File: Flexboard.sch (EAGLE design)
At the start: 353 parts, among them U1 MK20DN512VLQ10

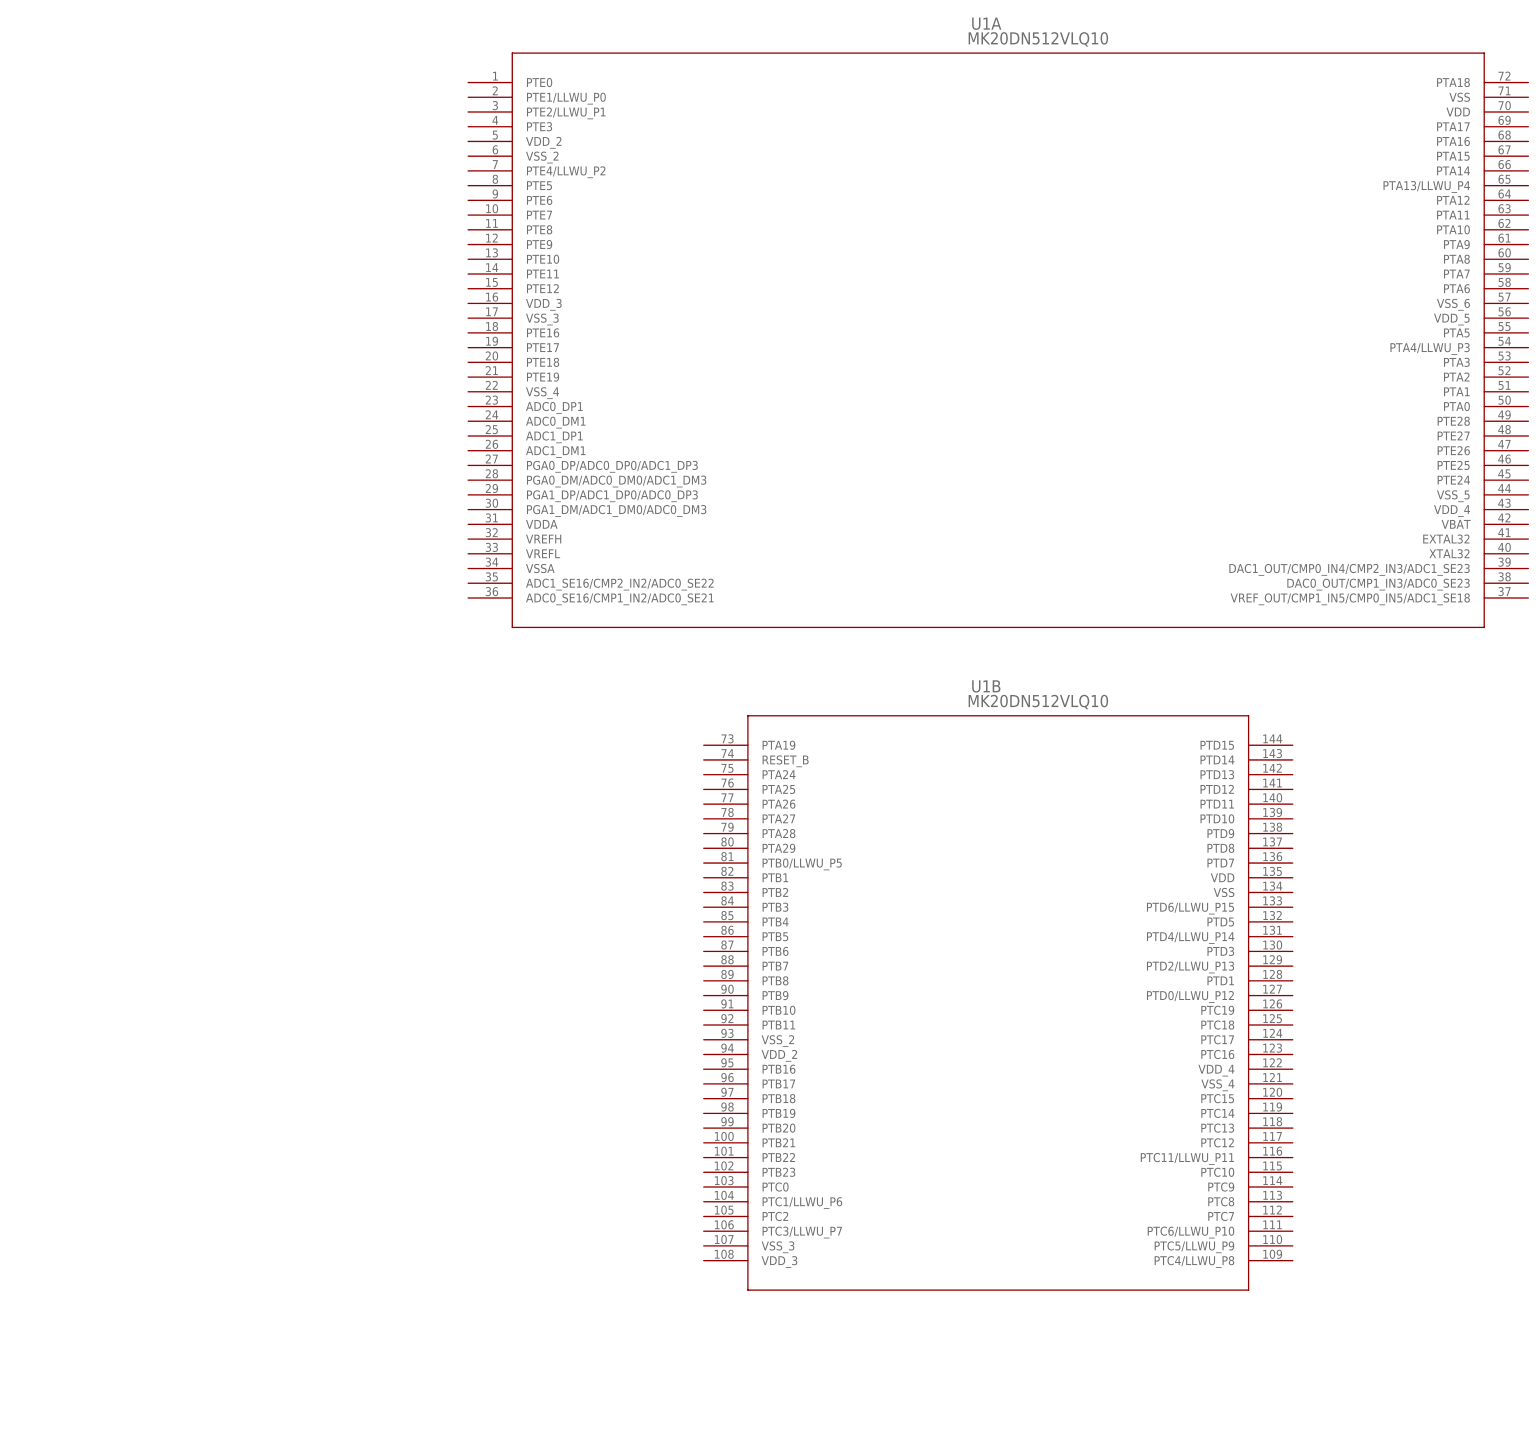
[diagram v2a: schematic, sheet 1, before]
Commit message: Assigned all keyboard traces to pins on MCU
All traces for columns and rows now have initial pin assignments
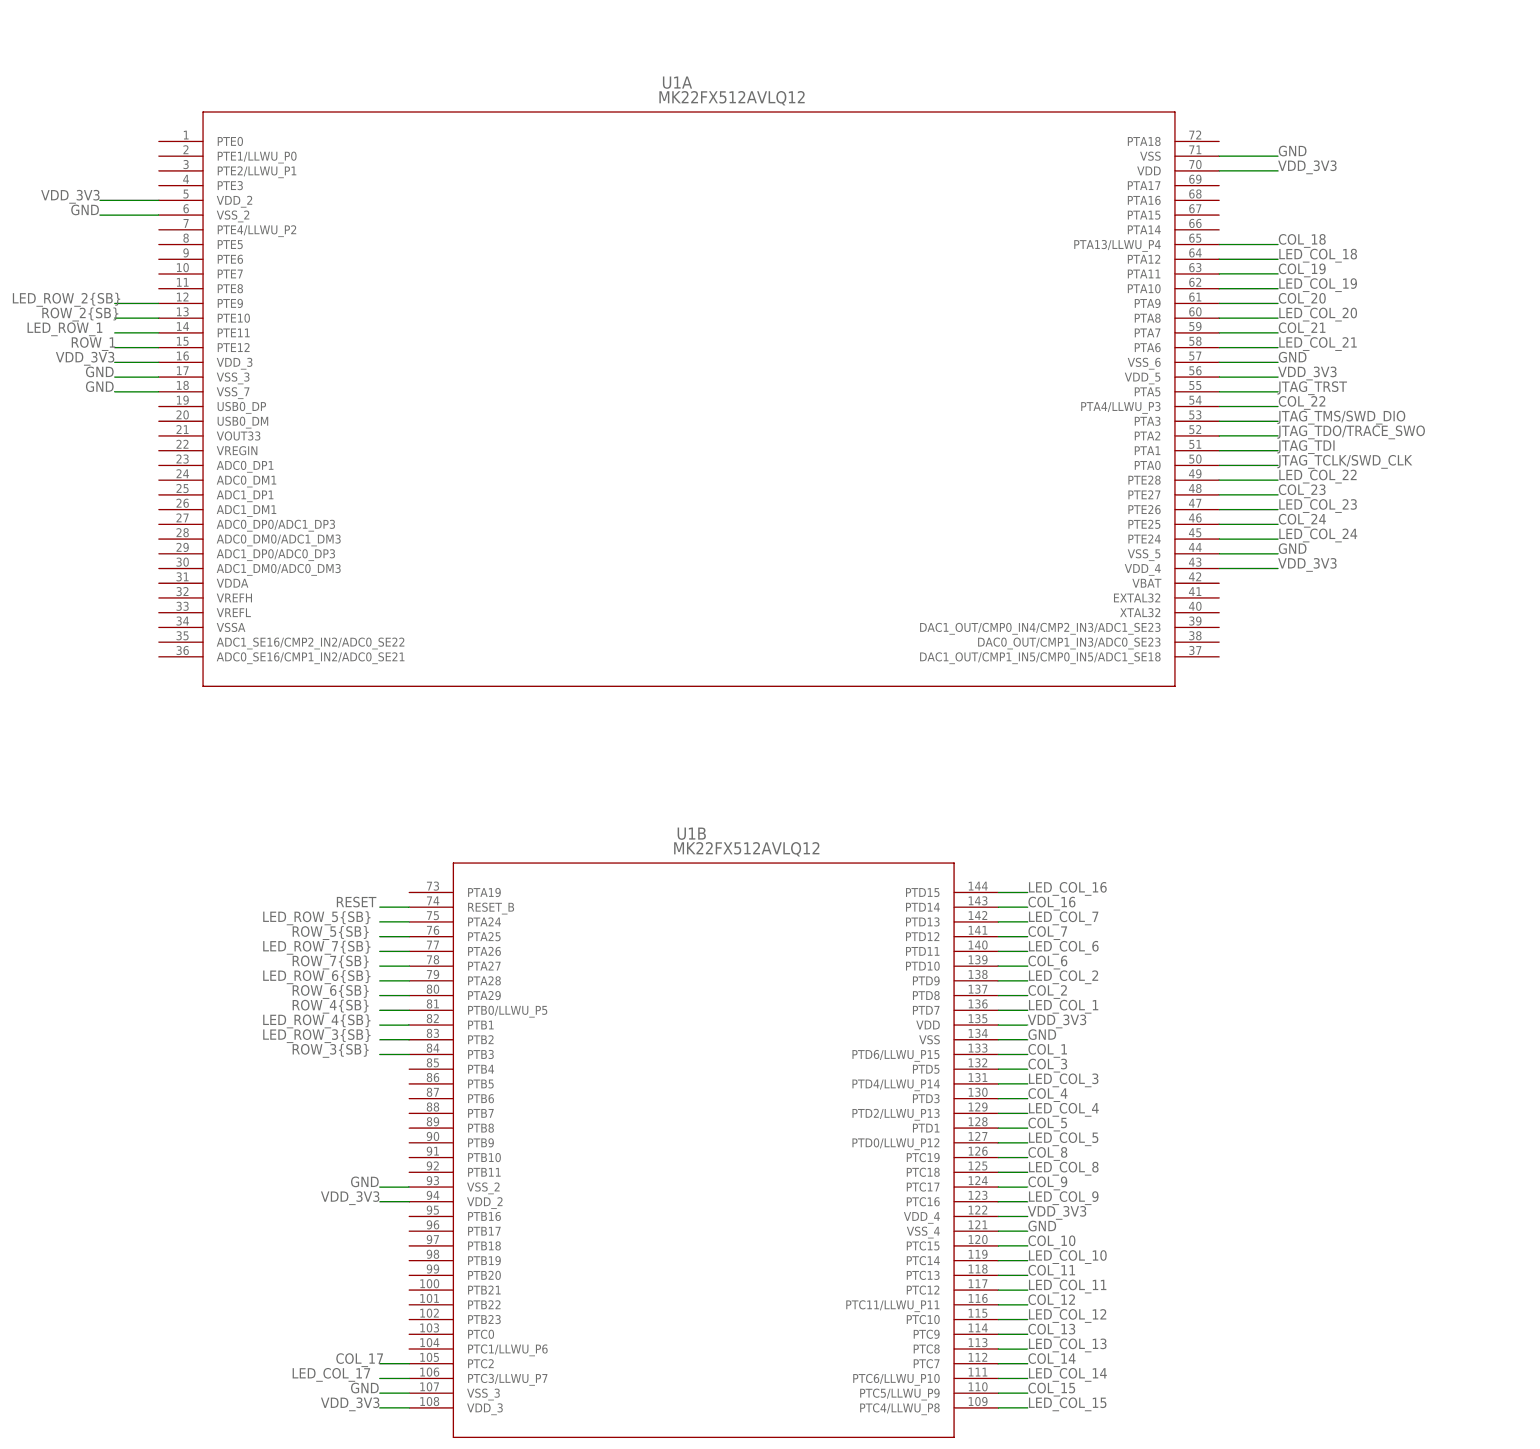
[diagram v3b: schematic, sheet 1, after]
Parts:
- U1: value MK20DN512VLQ10 -> MK22FX512AVLQ12; device MK20DN512VLQ10:MK20DN512VLQ10 -> MK22FX512AVLQ12:MK22FX512AVLQ12
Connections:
- removed net LED_ROW_2B: KEY_23.LED+, KEY_24.LED+, KEY_25.LED+, KEY_26.LED+, KEY_27.LED+, KEY_28.LED+, KEY_29.LED+, KEY_30.LED+, KEY_30_OFFSET.LED+, KEY_31.LED+, KEY_31_OFFSET.LED+, KEY_32.LED+, KEY_32_OFFSET.LED+, KEY_33.LED+, KEY_33_OFFSET.LED+, KEY_34.LED+, KEY_35.LED+, KEY_36.LED+, KEY_37.LED+, KEY_38.LED+, KEY_39.LED+, KEY_40.LED+, SJ_LED_R2_0.1
- removed net LED_ROW_3B: KEY_43.LED+, KEY_44.LED+, KEY_45.LED+, KEY_46.LED+, KEY_47.LED+, KEY_48.LED+, KEY_49.LED+, KEY_50.LED+, KEY_51.LED+, KEY_52.LED+, KEY_53.LED+, KEY_54.LED+, KEY_55.LED+, KEY_56.LED+, KEY_57.LED+, KEY_58.LED+, KEY_59.LED+, SJ_LED_R3_0.1, SJ_LED_R3_1.2
- removed net LED_ROW_4B: KEY_66.LED+, KEY_67.LED+, KEY_68.LED+, KEY_69.LED+, KEY_70.LED+, KEY_71.LED+, KEY_72.LED+, KEY_73.LED+, KEY_74.LED+, KEY_75.LED+, KEY_76.LED+, KEY_77.LED+, KEY_78.LED+, KEY_79.LED+, KEY_80.LED+, KEY_81.LED+, KEY_82.LED+, SJ_LED_R4_1.2, SJ__LED_R4_0.1
- removed net LED_ROW_5B: KEY_100.LED+, KEY_101.LED+, KEY_102.LED+, KEY_103.LED+, KEY_104.LED+, KEY_89.LED+, KEY_90.LED+, KEY_91.LED+, KEY_92.LED+, KEY_93.LED+, KEY_94.LED+, KEY_95.LED+, KEY_96.LED+, KEY_97.LED+, KEY_98.LED+, KEY_99.LED+, SJ_LED_R5_0.1, SJ_LED_R5_1.2
- removed net LED_ROW_6B: KEY_111.LED+, KEY_112.LED+, KEY_113.LED+, KEY_114.LED+, KEY_115.LED+, KEY_116.LED+, KEY_117.LED+, KEY_118.LED+, KEY_119.LED+, KEY_120.LED+, KEY_121.LED+, KEY_122.LED+, KEY_123.LED+, KEY_124.LED+, KEY_125.LED+, SJ_LED_R6_0.1, SJ_LED_R6_1.2
- removed net LED_ROW_7B: KEY_131.LED+, KEY_132.LED+, KEY_133.LED+, KEY_134.LED+, KEY_135.LED+, KEY_136.LED+, KEY_137.LED+, KEY_138.LED+, KEY_139.LED+, KEY_140.LED+, KEY_141.LED+, SJ_LED_R7_0.1, SJ_LED_R7_1.2
- removed net ROW_2B: D23.A, D24.A, D25.A, D26.A, D27.A, D28.A, D29.A, D30.A, D31.A, D32.A, D33.A, D34.A, D35.A, D36.A, D37.A, D38.A, D39.A, D40.A, SJ_R2_0.1
- removed net ROW_3B: D43.A, D44.A, D45.A, D46.A, D47.A, D48.A, D49.A, D50.A, D51.A, D52.A, D53.A, D54.A, D55.A, D56.A, D57.A, D58.A, D59.A, SJ_R3_0.1, SJ_R3_1.2
- removed net ROW_4B: D66.A, D67.A, D68.A, D69.A, D70.A, D71.A, D72.A, D73.A, D74.A, D75.A, D76.A, D77.A, D78.A, D79.A, D80.A, D81.A, D82.A, SJ_R4_0.1, SJ_R4_1.2
- removed net ROW_5B: D100.A, D101.A, D102.A, D103.A, D104.A, D89.A, D90.A, D91.A, D92.A, D93.A, D94.A, D95.A, D96.A, D97.A, D98.A, D99.A, SJ_R5_0.1, SJ_R5_1.2
- removed net ROW_6B: D111.A, D112.A, D113.A, D114.A, D115.A, D116.A, D117.A, D118.A, D119.A, D120.A, D121.A, D122.A, D123.A, D124.A, D125.A, SJ_R6_0.1, SJ_R6_1.2
- removed net ROW_7B: D131.A, D132.A, D133.A, D134.A, D135.A, D136.A, D137.A, D138.A, D139.A, D140.A, D141.A, SJ_R7_0.1, SJ_R7_1.2
- new net GND: U1A.VSS, U1A.VSS_2, U1A.VSS_3, U1A.VSS_5, U1A.VSS_6, U1A.VSS_7, U1B.VSS, U1B.VSS_2, U1B.VSS_3, U1B.VSS_4
- new net JTAG_TCLK/SWD_CLK: U1A.PTA0
- new net JTAG_TDI: U1A.PTA1
- new net JTAG_TDO/TRACE_SWO: U1A.PTA2
- new net JTAG_TMS/SWD_DIO: U1A.PTA3
- new net JTAG_TRST: U1A.PTA5
- new net LED_ROW_2{SB}: KEY_23.LED+, KEY_24.LED+, KEY_25.LED+, KEY_26.LED+, KEY_27.LED+, KEY_28.LED+, KEY_29.LED+, KEY_30.LED+, KEY_30_OFFSET.LED+, KEY_31.LED+, KEY_31_OFFSET.LED+, KEY_32.LED+, KEY_32_OFFSET.LED+, KEY_33.LED+, KEY_33_OFFSET.LED+, KEY_34.LED+, KEY_35.LED+, KEY_36.LED+, KEY_37.LED+, KEY_38.LED+, KEY_39.LED+, KEY_40.LED+, SJ_LED_R2_0.1, U1A.PTE9
- new net LED_ROW_3{SB}: KEY_43.LED+, KEY_44.LED+, KEY_45.LED+, KEY_46.LED+, KEY_47.LED+, KEY_48.LED+, KEY_49.LED+, KEY_50.LED+, KEY_51.LED+, KEY_52.LED+, KEY_53.LED+, KEY_54.LED+, KEY_55.LED+, KEY_56.LED+, KEY_57.LED+, KEY_58.LED+, KEY_59.LED+, SJ_LED_R3_0.1, SJ_LED_R3_1.2, U1B.PTB2
- new net LED_ROW_4{SB}: KEY_66.LED+, KEY_67.LED+, KEY_68.LED+, KEY_69.LED+, KEY_70.LED+, KEY_71.LED+, KEY_72.LED+, KEY_73.LED+, KEY_74.LED+, KEY_75.LED+, KEY_76.LED+, KEY_77.LED+, KEY_78.LED+, KEY_79.LED+, KEY_80.LED+, KEY_81.LED+, KEY_82.LED+, SJ_LED_R4_1.2, SJ__LED_R4_0.1, U1B.PTB1
- new net LED_ROW_5{SB}: KEY_100.LED+, KEY_101.LED+, KEY_102.LED+, KEY_103.LED+, KEY_104.LED+, KEY_89.LED+, KEY_90.LED+, KEY_91.LED+, KEY_92.LED+, KEY_93.LED+, KEY_94.LED+, KEY_95.LED+, KEY_96.LED+, KEY_97.LED+, KEY_98.LED+, KEY_99.LED+, SJ_LED_R5_0.1, SJ_LED_R5_1.2, U1B.PTA24
- new net LED_ROW_6{SB}: KEY_111.LED+, KEY_112.LED+, KEY_113.LED+, KEY_114.LED+, KEY_115.LED+, KEY_116.LED+, KEY_117.LED+, KEY_118.LED+, KEY_119.LED+, KEY_120.LED+, KEY_121.LED+, KEY_122.LED+, KEY_123.LED+, KEY_124.LED+, KEY_125.LED+, SJ_LED_R6_0.1, SJ_LED_R6_1.2, U1B.PTA28
- new net LED_ROW_7{SB}: KEY_131.LED+, KEY_132.LED+, KEY_133.LED+, KEY_134.LED+, KEY_135.LED+, KEY_136.LED+, KEY_137.LED+, KEY_138.LED+, KEY_139.LED+, KEY_140.LED+, KEY_141.LED+, SJ_LED_R7_0.1, SJ_LED_R7_1.2, U1B.PTA26
- new net RESET: U1B.RESET_B
- new net ROW_2{SB}: D23.A, D24.A, D25.A, D26.A, D27.A, D28.A, D29.A, D30.A, D31.A, D32.A, D33.A, D34.A, D35.A, D36.A, D37.A, D38.A, D39.A, D40.A, SJ_R2_0.1, U1A.PTE10
- new net ROW_3{SB}: D43.A, D44.A, D45.A, D46.A, D47.A, D48.A, D49.A, D50.A, D51.A, D52.A, D53.A, D54.A, D55.A, D56.A, D57.A, D58.A, D59.A, SJ_R3_0.1, SJ_R3_1.2, U1B.PTB3
- new net ROW_4{SB}: D66.A, D67.A, D68.A, D69.A, D70.A, D71.A, D72.A, D73.A, D74.A, D75.A, D76.A, D77.A, D78.A, D79.A, D80.A, D81.A, D82.A, SJ_R4_0.1, SJ_R4_1.2, U1B.PTB0/LLWU_P5
- new net ROW_5{SB}: D100.A, D101.A, D102.A, D103.A, D104.A, D89.A, D90.A, D91.A, D92.A, D93.A, D94.A, D95.A, D96.A, D97.A, D98.A, D99.A, SJ_R5_0.1, SJ_R5_1.2, U1B.PTA25
- new net ROW_6{SB}: D111.A, D112.A, D113.A, D114.A, D115.A, D116.A, D117.A, D118.A, D119.A, D120.A, D121.A, D122.A, D123.A, D124.A, D125.A, SJ_R6_0.1, SJ_R6_1.2, U1B.PTA29
- new net ROW_7{SB}: D131.A, D132.A, D133.A, D134.A, D135.A, D136.A, D137.A, D138.A, D139.A, D140.A, D141.A, SJ_R7_0.1, SJ_R7_1.2, U1B.PTA27
- new net VDD_3V3: U1A.VDD, U1A.VDD_2, U1A.VDD_3, U1A.VDD_4, U1A.VDD_5, U1B.VDD, U1B.VDD_2, U1B.VDD_3, U1B.VDD_4
- net COL_1: now also U1B.PTD6/LLWU_P15
- net COL_10: now also U1B.PTC15
- net COL_11: now also U1B.PTC13
- net COL_12: now also U1B.PTC11/LLWU_P11
- net COL_13: now also U1B.PTC9
- net COL_14: now also U1B.PTC7
- net COL_15: now also U1B.PTC5/LLWU_P9
- net COL_16: now also U1B.PTD14
- net COL_17: now also U1B.PTC2
- net COL_18: now also U1A.PTA13/LLWU_P4
- net COL_19: now also U1A.PTA11
- net COL_2: now also U1B.PTD8
- net COL_20: now also U1A.PTA9
- net COL_21: now also U1A.PTA7
- net COL_22: now also U1A.PTA4/LLWU_P3
- net COL_23: now also U1A.PTE27
- net COL_24: now also U1A.PTE25
- net COL_3: now also U1B.PTD5
- net COL_4: now also U1B.PTD3
- net COL_5: now also U1B.PTD1
- net COL_6: now also U1B.PTD10
- net COL_7: now also U1B.PTD12
- net COL_8: now also U1B.PTC19
- net COL_9: now also U1B.PTC17
- net LED_COL_1: now also U1B.PTD7
- net LED_COL_10: now also U1B.PTC14
- net LED_COL_11: now also U1B.PTC12
- net LED_COL_12: now also U1B.PTC10
- net LED_COL_13: now also U1B.PTC8
- net LED_COL_14: now also U1B.PTC6/LLWU_P10
- net LED_COL_15: now also U1B.PTC4/LLWU_P8
- net LED_COL_16: now also U1B.PTD15
- net LED_COL_17: now also U1B.PTC3/LLWU_P7
- net LED_COL_18: now also U1A.PTA12
- net LED_COL_19: now also U1A.PTA10
- net LED_COL_2: now also U1B.PTD9
- net LED_COL_20: now also U1A.PTA8
- net LED_COL_21: now also U1A.PTA6
- net LED_COL_22: now also U1A.PTE28
- net LED_COL_23: now also U1A.PTE26
- net LED_COL_24: now also U1A.PTE24
- net LED_COL_3: now also U1B.PTD4/LLWU_P14
- net LED_COL_4: now also U1B.PTD2/LLWU_P13
- net LED_COL_5: now also U1B.PTD0/LLWU_P12
- net LED_COL_6: now also U1B.PTD11
- net LED_COL_7: now also U1B.PTD13
- net LED_COL_8: now also U1B.PTC18
- net LED_COL_9: now also U1B.PTC16
- net LED_ROW_1: now also U1A.PTE11
- net ROW_1: now also U1A.PTE12
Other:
- moved on the sheet: U1A, U1B

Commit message: Added jumpers on each column and row trace
Column and row traces now have jumpers, which are normally
closed. These jumpers can be used to fix any routing errors,
by cutting the jumper and patching wires.
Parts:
- added SJ_C1, SJ_C2, SJ_LED_C1, SJ_LED_C2, SJ_LED_R1, SJ_R1: (no value), jumper:SJW
- added SJ_MCU_COL1, SJ_MCU_COL10, SJ_MCU_COL11, SJ_MCU_COL12, SJ_MCU_COL13, SJ_MCU_COL14, SJ_MCU_COL15, SJ_MCU_COL16, SJ_MCU_COL17, SJ_MCU_COL18, SJ_MCU_COL19, SJ_MCU_COL2, SJ_MCU_COL20, SJ_MCU_COL21, SJ_MCU_COL22, SJ_MCU_COL23, SJ_MCU_COL24, SJ_MCU_COL3, SJ_MCU_COL4, SJ_MCU_COL5, SJ_MCU_COL6, SJ_MCU_COL7, SJ_MCU_COL8, SJ_MCU_COL9, SJ_MCU_LED_COL1, SJ_MCU_LED_COL10, SJ_MCU_LED_COL11, SJ_MCU_LED_COL12, SJ_MCU_LED_COL13, SJ_MCU_LED_COL14, SJ_MCU_LED_COL15, SJ_MCU_LED_COL16, SJ_MCU_LED_COL17, SJ_MCU_LED_COL18, SJ_MCU_LED_COL19, SJ_MCU_LED_COL2, SJ_MCU_LED_COL20, SJ_MCU_LED_COL21, SJ_MCU_LED_COL22, SJ_MCU_LED_COL23, SJ_MCU_LED_COL24, SJ_MCU_LED_COL3, SJ_MCU_LED_COL4, SJ_MCU_LED_COL5, SJ_MCU_LED_COL6, SJ_MCU_LED_COL7, SJ_MCU_LED_COL8, SJ_MCU_LED_COL9, SJ_MCU_LED_ROW1, SJ_MCU_LED_ROW2, SJ_MCU_LED_ROW3, SJ_MCU_LED_ROW4, SJ_MCU_LED_ROW5, SJ_MCU_LED_ROW6, SJ_MCU_LED_ROW7, SJ_MCU_ROW1, SJ_MCU_ROW2, SJ_MCU_ROW3, SJ_MCU_ROW4, SJ_MCU_ROW5, SJ_MCU_ROW6, SJ_MCU_ROW7: JUMPER-SMT_2_NC_TRACE_NO-SILK, SparkFun-Jumpers:JUMPER-SMT_2_NC_TRACE_NO-SILK
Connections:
- new net COL_10{MCU}: SJ_MCU_COL10.2, U1B.PTC15
- new net COL_11{MCU}: SJ_MCU_COL11.2, U1B.PTC13
- new net COL_12{MCU}: SJ_MCU_COL12.2, U1B.PTC11/LLWU_P11
- new net COL_13{MCU}: SJ_MCU_COL13.2, U1B.PTC9
- new net COL_14{MCU}: SJ_MCU_COL14.2, U1B.PTC7
- new net COL_15{MCU}: SJ_MCU_COL15.2, U1B.PTC5/LLWU_P9
- new net COL_16{MCU}: SJ_MCU_COL16.2, U1B.PTD14
- new net COL_17{MCU}: SJ_MCU_COL17.2, U1B.PTC2
- new net COL_18{MCU}: SJ_MCU_COL18.2, U1A.PTA13/LLWU_P4
- new net COL_19{MCU}: SJ_MCU_COL19.2, U1A.PTA11
- new net COL_1{MCU}: SJ_MCU_COL1.2, U1B.PTD6/LLWU_P15
- new net COL_1{SB}: KEY_1.SW1, KEY_109.SW1, KEY_129.SW1, KEY_21.SW1, KEY_41.SW1, KEY_64.SW1, KEY_87.SW1, SJ_C1.1
- new net COL_20{MCU}: SJ_MCU_COL20.2, U1A.PTA9
- new net COL_21{MCU}: SJ_MCU_COL21.2, U1A.PTA7
- new net COL_22{MCU}: SJ_MCU_COL22.2, U1A.PTA4/LLWU_P3
- new net COL_23{MCU}: SJ_MCU_COL23.2, U1A.PTE27
- new net COL_24{MCU}: SJ_MCU_COL24.2, U1A.PTE25
- new net COL_2{MCU}: SJ_MCU_COL2.2, U1B.PTD8
- new net COL_2{SB}: KEY_110.SW1, KEY_130.SW1, KEY_2.SW1, KEY_22.SW1, KEY_42.SW1, KEY_65.SW1, KEY_88.SW1, SJ_C2.1
- new net COL_3{MCU}: SJ_MCU_COL3.2, U1B.PTD5
- new net COL_4{MCU}: SJ_MCU_COL4.2, U1B.PTD3
- new net COL_5{MCU}: SJ_MCU_COL5.2, U1B.PTD1
- new net COL_6{MCU}: SJ_MCU_COL6.2, U1B.PTD10
- new net COL_7{MCU}: SJ_MCU_COL7.2, U1B.PTD12
- new net COL_8{MCU}: SJ_MCU_COL8.2, U1B.PTC19
- new net COL_9{MCU}: SJ_MCU_COL9.2, U1B.PTC17
- new net LED_COL_10{MCU}: SJ_MCU_LED_COL10.2, U1B.PTC14
- new net LED_COL_11{MCU}: SJ_MCU_LED_COL11.2, U1B.PTC12
- new net LED_COL_12{MCU}: SJ_MCU_LED_COL12.2, U1B.PTC10
- new net LED_COL_13{MCU}: SJ_MCU_LED_COL13.2, U1B.PTC8
- new net LED_COL_14{MCU}: SJ_MCU_LED_COL14.2, U1B.PTC6/LLWU_P10
- new net LED_COL_15{MCU}: SJ_MCU_LED_COL15.2, U1B.PTC4/LLWU_P8
- new net LED_COL_16{MCU}: SJ_MCU_LED_COL16.2, U1B.PTD15
- new net LED_COL_17{MCU}: SJ_MCU_LED_COL17.2, U1B.PTC3/LLWU_P7
- new net LED_COL_18{MCU}: SJ_MCU_LED_COL18.2, U1A.PTA12
- new net LED_COL_19{MCU}: SJ_MCU_LED_COL19.2, U1A.PTA10
- new net LED_COL_1{MCU}: SJ_MCU_LED_COL1.2, U1B.PTD7
- new net LED_COL_1{SB}: KEY_1.LED-, KEY_109.LED-, KEY_129.LED-, KEY_21.LED-, KEY_41.LED-, KEY_64.LED-, KEY_87.LED-, SJ_LED_C1.1
- new net LED_COL_20{MCU}: SJ_MCU_LED_COL20.2, U1A.PTA8
- new net LED_COL_21{MCU}: SJ_MCU_LED_COL21.2, U1A.PTA6
- new net LED_COL_22{MCU}: SJ_MCU_LED_COL22.2, U1A.PTE28
- new net LED_COL_23{MCU}: SJ_MCU_LED_COL23.2, U1A.PTE26
- new net LED_COL_24{MCU}: SJ_MCU_LED_COL24.2, U1A.PTE24
- new net LED_COL_2{MCU}: SJ_MCU_LED_COL2.2, U1B.PTD9
- new net LED_COL_2{SB}: KEY_110.LED-, KEY_130.LED-, KEY_2.LED-, KEY_22.LED-, KEY_42.LED-, KEY_65.LED-, KEY_88.LED-, SJ_LED_C2.1
- new net LED_COL_3{MCU}: SJ_MCU_LED_COL3.2, U1B.PTD4/LLWU_P14
- new net LED_COL_4{MCU}: SJ_MCU_LED_COL4.2, U1B.PTD2/LLWU_P13
- new net LED_COL_5{MCU}: SJ_MCU_LED_COL5.2, U1B.PTD0/LLWU_P12
- new net LED_COL_6{MCU}: SJ_MCU_LED_COL6.2, U1B.PTD11
- new net LED_COL_7{MCU}: SJ_MCU_LED_COL7.2, U1B.PTD13
- new net LED_COL_8{MCU}: SJ_MCU_LED_COL8.2, U1B.PTC18
- new net LED_COL_9{MCU}: SJ_MCU_LED_COL9.2, U1B.PTC16
- new net LED_ROW_1{MCU}: SJ_MCU_LED_ROW1.2, U1A.PTE11
- new net LED_ROW_1{SB}: SJ_LED_R1.2, SJ_MCU_LED_ROW1.1
- new net LED_ROW_2{MCU}: SJ_MCU_LED_ROW2.2, U1A.PTE9
- new net LED_ROW_3{MCU}: SJ_MCU_LED_ROW3.2, U1B.PTB2
- new net LED_ROW_4{MCU}: SJ_MCU_LED_ROW4.2, U1B.PTB1
- new net LED_ROW_5{MCU}: SJ_MCU_LED_ROW5.2, U1B.PTA24
- new net LED_ROW_6{MCU}: SJ_MCU_LED_ROW6.2, U1B.PTA28
- new net LED_ROW_7{MCU}: SJ_MCU_LED_ROW7.2, U1B.PTA26
- new net ROW_1{MCU}: SJ_MCU_ROW1.2, U1A.PTE12
- new net ROW_1{SB}: SJ_MCU_ROW1.1, SJ_R1.2
- new net ROW_2{MCU}: SJ_MCU_ROW2.2, U1A.PTE10
- new net ROW_3{MCU}: SJ_MCU_ROW3.2, U1B.PTB3
- new net ROW_4{MCU}: SJ_MCU_ROW4.2, U1B.PTB0/LLWU_P5
- new net ROW_5{MCU}: SJ_MCU_ROW5.2, U1B.PTA25
- new net ROW_6{MCU}: SJ_MCU_ROW6.2, U1B.PTA29
- new net ROW_7{MCU}: SJ_MCU_ROW7.2, U1B.PTA27
- net COL_1: now also SJ_C1.2, SJ_MCU_COL1.1; no longer KEY_1.SW1, KEY_109.SW1, KEY_129.SW1, KEY_21.SW1, KEY_41.SW1, KEY_64.SW1, KEY_87.SW1, U1B.PTD6/LLWU_P15
- net COL_10: now also SJ_MCU_COL10.1; no longer U1B.PTC15
- net COL_11: now also SJ_MCU_COL11.1; no longer U1B.PTC13
- net COL_12: now also SJ_MCU_COL12.1; no longer U1B.PTC11/LLWU_P11
- net COL_13: now also SJ_MCU_COL13.1; no longer U1B.PTC9
- net COL_14: now also SJ_MCU_COL14.1; no longer U1B.PTC7
- net COL_15: now also SJ_MCU_COL15.1; no longer U1B.PTC5/LLWU_P9
- net COL_16: now also SJ_MCU_COL16.1; no longer U1B.PTD14
- net COL_17: now also SJ_MCU_COL17.1; no longer U1B.PTC2
- net COL_18: now also SJ_MCU_COL18.1; no longer U1A.PTA13/LLWU_P4
- net COL_19: now also SJ_MCU_COL19.1; no longer U1A.PTA11
- net COL_2: now also SJ_C2.2, SJ_MCU_COL2.1; no longer KEY_110.SW1, KEY_130.SW1, KEY_2.SW1, KEY_22.SW1, KEY_42.SW1, KEY_65.SW1, KEY_88.SW1, U1B.PTD8
- net COL_20: now also SJ_MCU_COL20.1; no longer U1A.PTA9
- net COL_21: now also SJ_MCU_COL21.1; no longer U1A.PTA7
- net COL_22: now also SJ_MCU_COL22.1; no longer U1A.PTA4/LLWU_P3
- net COL_23: now also SJ_MCU_COL23.1; no longer U1A.PTE27
- net COL_24: now also SJ_MCU_COL24.1; no longer U1A.PTE25
- net COL_3: now also SJ_MCU_COL3.1; no longer U1B.PTD5
- net COL_4: now also SJ_MCU_COL4.1; no longer U1B.PTD3
- net COL_5: now also SJ_MCU_COL5.1; no longer U1B.PTD1
- net COL_6: now also SJ_MCU_COL6.1; no longer U1B.PTD10
- net COL_7: now also SJ_MCU_COL7.1; no longer U1B.PTD12
- net COL_8: now also SJ_MCU_COL8.1; no longer U1B.PTC19
- net COL_9: now also SJ_MCU_COL9.1; no longer U1B.PTC17
- net LED_COL_1: now also SJ_LED_C1.2, SJ_MCU_LED_COL1.1; no longer KEY_1.LED-, KEY_109.LED-, KEY_129.LED-, KEY_21.LED-, KEY_41.LED-, KEY_64.LED-, KEY_87.LED-, U1B.PTD7
- net LED_COL_10: now also SJ_MCU_LED_COL10.1; no longer U1B.PTC14
- net LED_COL_11: now also SJ_MCU_LED_COL11.1; no longer U1B.PTC12
- net LED_COL_12: now also SJ_MCU_LED_COL12.1; no longer U1B.PTC10
- net LED_COL_13: now also SJ_MCU_LED_COL13.1; no longer U1B.PTC8
- net LED_COL_14: now also SJ_MCU_LED_COL14.1; no longer U1B.PTC6/LLWU_P10
- net LED_COL_15: now also SJ_MCU_LED_COL15.1; no longer U1B.PTC4/LLWU_P8
- net LED_COL_16: now also SJ_MCU_LED_COL16.1; no longer U1B.PTD15
- net LED_COL_17: now also SJ_MCU_LED_COL17.1; no longer U1B.PTC3/LLWU_P7
- net LED_COL_18: now also SJ_MCU_LED_COL18.1; no longer U1A.PTA12
- net LED_COL_19: now also SJ_MCU_LED_COL19.1; no longer U1A.PTA10
- net LED_COL_2: now also SJ_LED_C2.2, SJ_MCU_LED_COL2.1; no longer KEY_110.LED-, KEY_130.LED-, KEY_2.LED-, KEY_22.LED-, KEY_42.LED-, KEY_65.LED-, KEY_88.LED-, U1B.PTD9
- net LED_COL_20: now also SJ_MCU_LED_COL20.1; no longer U1A.PTA8
- net LED_COL_21: now also SJ_MCU_LED_COL21.1; no longer U1A.PTA6
- net LED_COL_22: now also SJ_MCU_LED_COL22.1; no longer U1A.PTE28
- net LED_COL_23: now also SJ_MCU_LED_COL23.1; no longer U1A.PTE26
- net LED_COL_24: now also SJ_MCU_LED_COL24.1; no longer U1A.PTE24
- net LED_COL_3: now also SJ_MCU_LED_COL3.1; no longer U1B.PTD4/LLWU_P14
- net LED_COL_4: now also SJ_MCU_LED_COL4.1; no longer U1B.PTD2/LLWU_P13
- net LED_COL_5: now also SJ_MCU_LED_COL5.1; no longer U1B.PTD0/LLWU_P12
- net LED_COL_6: now also SJ_MCU_LED_COL6.1; no longer U1B.PTD11
- net LED_COL_7: now also SJ_MCU_LED_COL7.1; no longer U1B.PTD13
- net LED_COL_8: now also SJ_MCU_LED_COL8.1; no longer U1B.PTC18
- net LED_COL_9: now also SJ_MCU_LED_COL9.1; no longer U1B.PTC16
- net LED_ROW_1: now also SJ_LED_R1.1; no longer U1A.PTE11
- net LED_ROW_2{SB}: now also SJ_MCU_LED_ROW2.1; no longer U1A.PTE9
- net LED_ROW_3{SB}: now also SJ_MCU_LED_ROW3.1; no longer U1B.PTB2
- net LED_ROW_4{SB}: now also SJ_MCU_LED_ROW4.1; no longer U1B.PTB1
- net LED_ROW_5{SB}: now also SJ_MCU_LED_ROW5.1; no longer U1B.PTA24
- net LED_ROW_6{SB}: now also SJ_MCU_LED_ROW6.1; no longer U1B.PTA28
- net LED_ROW_7{SB}: now also SJ_MCU_LED_ROW7.1; no longer U1B.PTA26
- net ROW_1: now also SJ_R1.1; no longer U1A.PTE12
- net ROW_2{SB}: now also SJ_MCU_ROW2.1; no longer U1A.PTE10
- net ROW_3{SB}: now also SJ_MCU_ROW3.1; no longer U1B.PTB3
- net ROW_4{SB}: now also SJ_MCU_ROW4.1; no longer U1B.PTB0/LLWU_P5
- net ROW_5{SB}: now also SJ_MCU_ROW5.1; no longer U1B.PTA25
- net ROW_6{SB}: now also SJ_MCU_ROW6.1; no longer U1B.PTA29
- net ROW_7{SB}: now also SJ_MCU_ROW7.1; no longer U1B.PTA27
